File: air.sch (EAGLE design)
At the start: 30 parts, among them IC2 LM2937, Q1 FC-12M, Q2 FC-26M, Q3 BC849SMD, Q4 BC849SMD, U1 ESP8266, U2 W25Q32FV

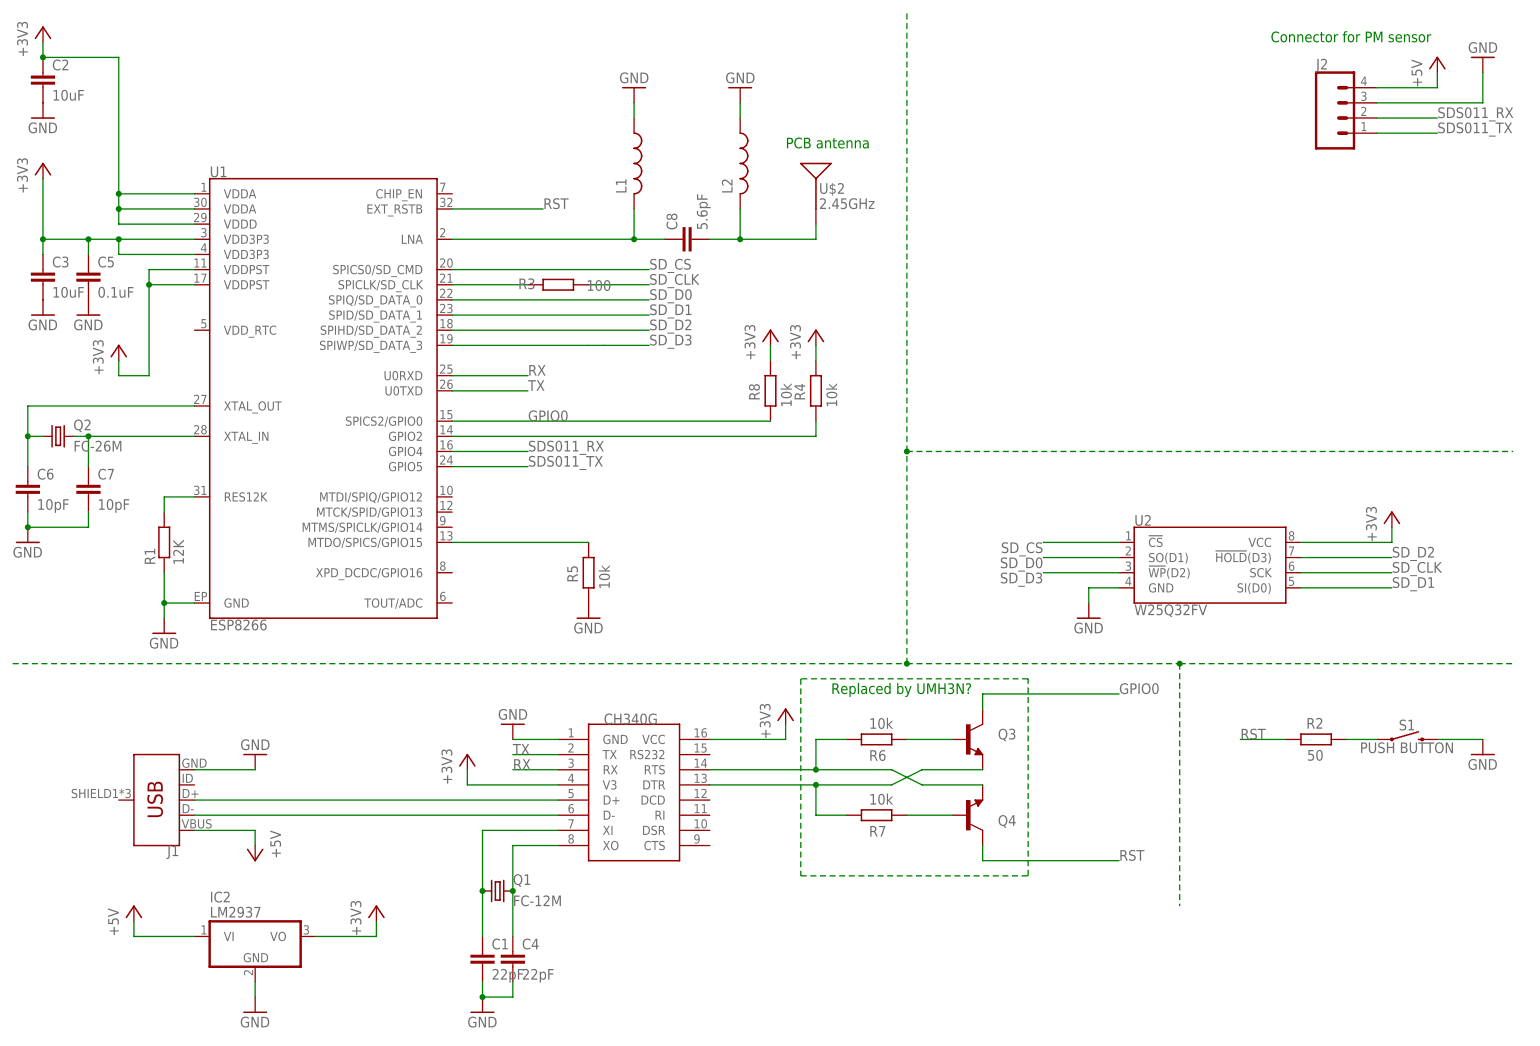
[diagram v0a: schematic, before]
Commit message: Switch to SMD, change voltage regulator, fix errors
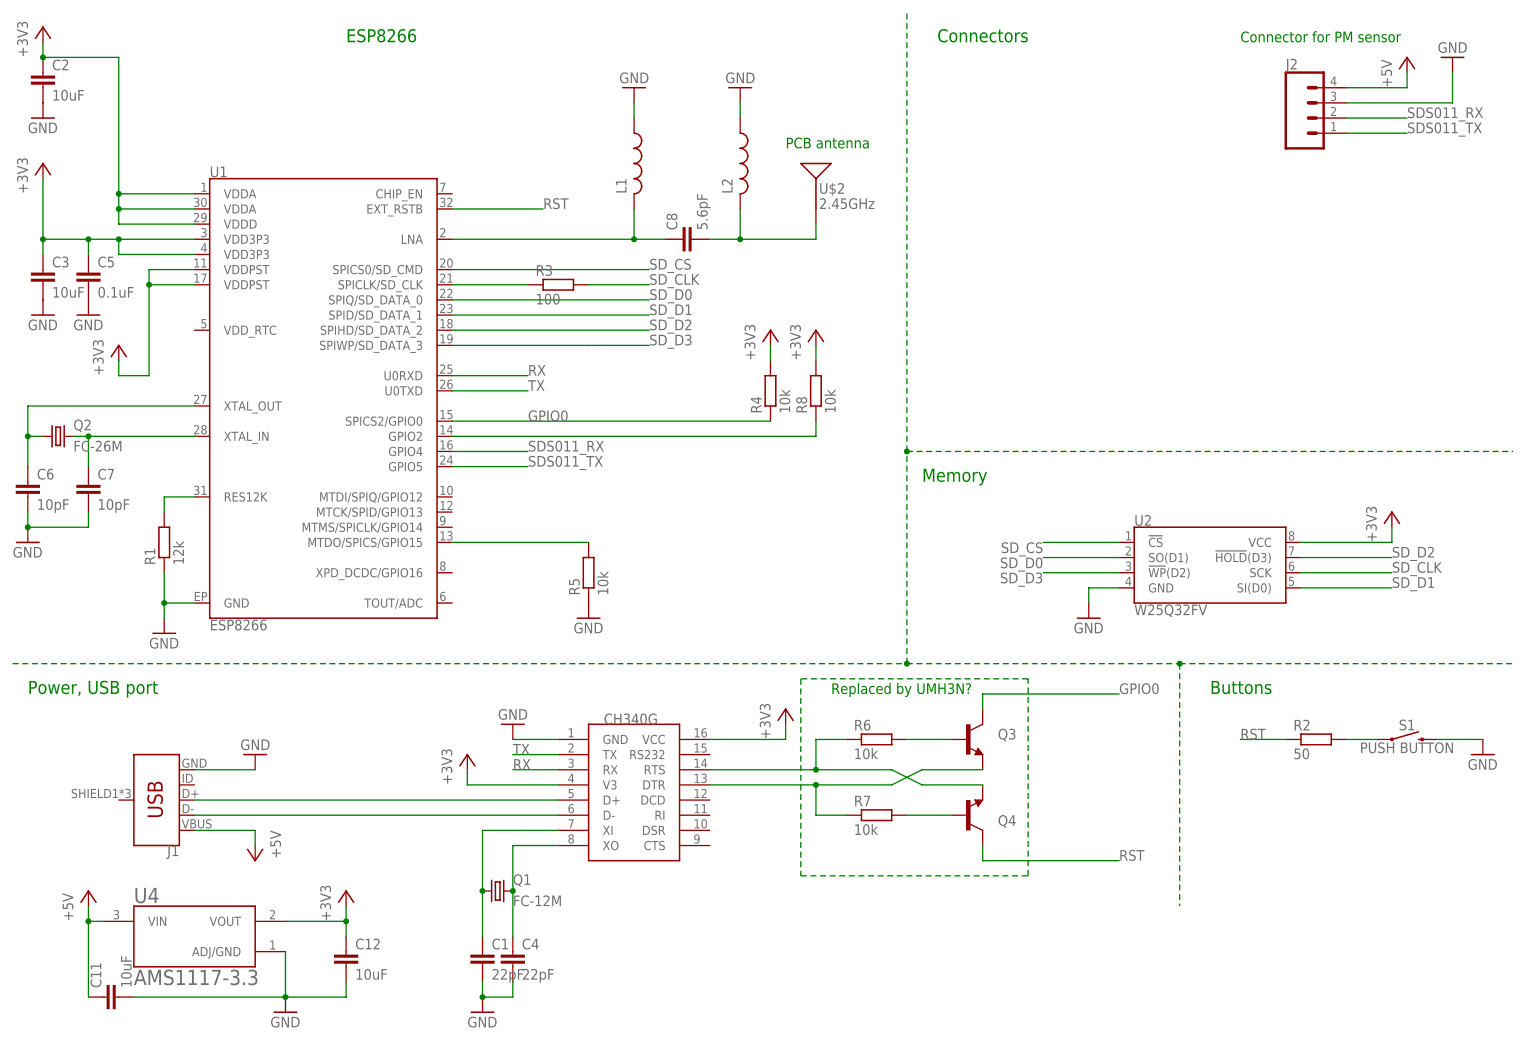
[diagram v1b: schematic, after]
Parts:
- removed IC2: LM2937, linear:LM2937
- added C11, C12: 10uF, rcl:C-EUC1206
- added U4: AMS1117-3.3, AMS1117-3.3:AMS1117-3.3
- L1, L2: device resistor:L-US0204/7 -> rcl:L-USL1812
- R1: value 12K -> 12k; device rcl:R-EU_0204/7 -> rcl:R-EU_R0805
- R2, R3, R4, R5, R6, R7, R8: device rcl:R-EU_0204/7 -> rcl:R-EU_R0805
- renumbered U$1 to U3
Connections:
- net +3V3: now also C12.1, R4.2, R8.2, U4.VOUT; no longer IC2.VO, R4.1, R8.1
- net +5V: now also C11.1, U4.VIN; no longer IC2.VI
- net GND: now also C11.2, C12.2, R5.1, U4.ADJ/GND; no longer IC2.GND, R5.2
- net GPIO0: now also R4.1; no longer R8.2
- net N$1: now also R3.1; no longer R3.2
- net N$12: now also R8.1; no longer R4.2
- net N$13: now also R5.2; no longer R5.1
- net N$9: now also R2.2; no longer R2.1
- net RST: now also R2.1; no longer R2.2
- net SD_CLK: now also R3.2; no longer R3.1
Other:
- note added: "Buttons"
- note added: "Connectors"
- note added: "ESP8266"
- note added: "Memory"
- note added: "Power, USB port"
- moved on the sheet: J2, R2, R3, R4, R5, R8

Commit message: Add capeboard schematic and led on main schematic
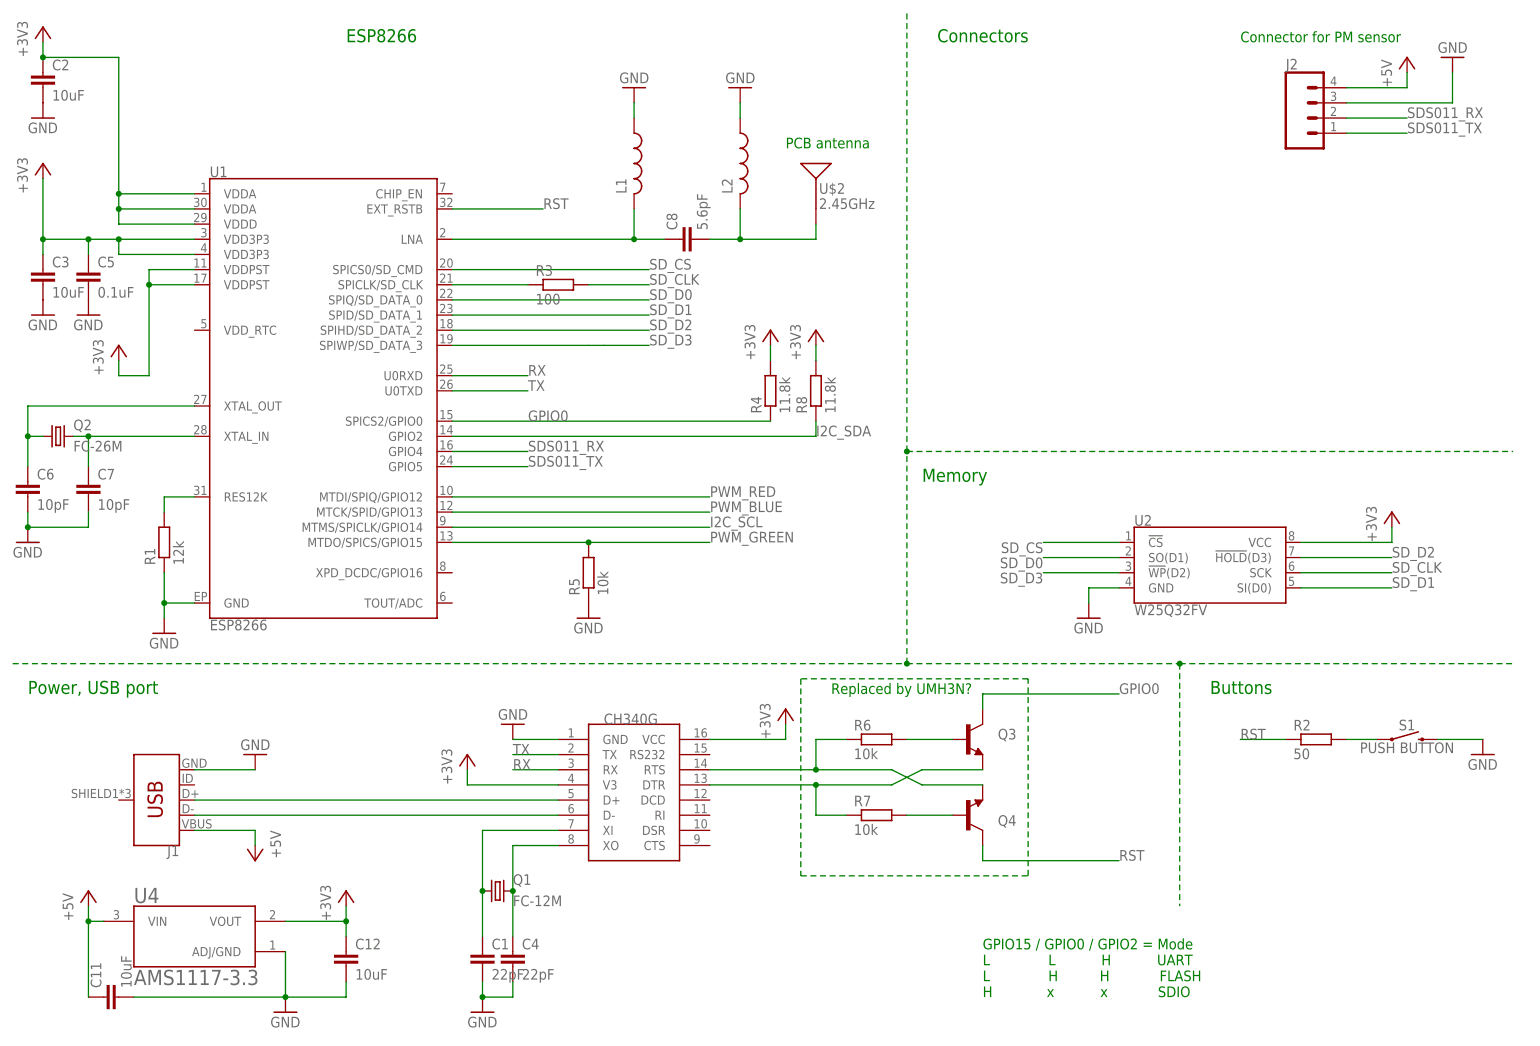
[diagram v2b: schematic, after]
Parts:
- R4, R8: value 10k -> 11.8k
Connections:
- net N$12 renamed I2C_SDA
- net N$13 renamed PWM_GREEN
- new net I2C_SCL: U1.MTMS/SPICLK/GPIO14
- new net PWM_RED: U1.MTDI/SPIQ/GPIO12
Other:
- note added: "GPIO15 / GPIO0 / GPIO2 = Mode L L H UART L H H FLASH H x x SDIO"
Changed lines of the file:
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@@
 <part name="GND15" library="supply1" library_urn="urn:adsk.eagle:library:371" deviceset="GND" device=""/>
 <part name="R3" library="rcl" library_urn="urn:adsk.eagle:library:334" deviceset="R-EU_" device="R0805" package3d_urn="urn:adsk.eagle:package:23553/2" value="100"/>
-<part name="R4" library="rcl" library_urn="urn:adsk.eagle:library:334" deviceset="R-EU_" device="R0805" package3d_urn="urn:adsk.eagle:package:23553/2" value="10k"/>
-<part name="R8" library="rcl" library_urn="urn:adsk.eagle:library:334" deviceset="R-EU_" device="R0805" package3d_urn="urn:adsk.eagle:package:23553/2" value="10k"/>
+<part name="R4" library="rcl" library_urn="urn:adsk.eagle:library:334" deviceset="R-EU_" device="R0805" package3d_urn="urn:adsk.eagle:package:23553/2" value="11.8k"/>
+<part name="R8" library="rcl" library_urn="urn:adsk.eagle:library:334" deviceset="R-EU_" device="R0805" package3d_urn="urn:adsk.eagle:package:23553/2" value="11.8k"/>
 <part name="R5" library="rcl" library_urn="urn:adsk.eagle:library:334" deviceset="R-EU_" device="R0805" package3d_urn="urn:adsk.eagle:package:23553/2" value="10k"/>
 <part name="R1" library="rcl" library_urn="urn:adsk.eagle:library:334" deviceset="R-EU_" device="R0805" package3d_urn="urn:adsk.eagle:package:23553/2" value="12k"/>
@@
 <text x="160.02" y="170.18" size="2.1844" layer="91">Connectors</text>
 <text x="205.74" y="60.96" size="2.1844" layer="91">Buttons</text>
+<text x="167.64" y="10.16" size="1.778" layer="91">GPIO15 / GPIO0 / GPIO2 = Mode
+L              L           H           UART
+L              H          H            FLASH
+H             x           x            SDIO</text>
 </plain>
 <instances>
@@
 </segment>
 </net>
-<net name="N$12" class="0">
+<net name="I2C_SDA" class="0">
 <segment>
 <pinref part="U1" gate="G$1" pin="GPIO2"/>
@@
 <wire x1="139.7" y1="104.14" x2="139.7" y2="106.68" width="0.1524" layer="91"/>
 <pinref part="R8" gate="G$1" pin="1"/>
-</segment>
-</net>
-<net name="N$13" class="0">
+<label x="139.7" y="104.14" size="1.778" layer="95"/>
+</segment>
+</net>
+<net name="PWM_GREEN" class="0">
 <segment>
 <pinref part="U1" gate="G$1" pin="MTDO/SPICS/GPIO15"/>
 <wire x1="78.74" y1="86.36" x2="101.6" y2="86.36" width="0.1524" layer="91"/>
 <pinref part="R5" gate="G$1" pin="2"/>
+<wire x1="101.6" y1="86.36" x2="121.92" y2="86.36" width="0.1524" layer="91"/>
+<junction x="101.6" y="86.36"/>
+<label x="121.92" y="86.36" size="1.778" layer="95"/>
 </segment>
 </net>
@@
 </segment>
 </net>
+<net name="PWM_RED" class="0">
+<segment>
+<pinref part="U1" gate="G$1" pin="MTDI/SPIQ/GPIO12"/>
+<wire x1="78.74" y1="93.98" x2="121.92" y2="93.98" width="0.1524" layer="91"/>
+<label x="121.92" y="93.98" size="1.778" layer="95"/>
+</segment>
+</net>
+<net name="PWM_BLUE" class="0">
+<segment>
+<wire x1="78.74" y1="91.44" x2="121.92" y2="91.44" width="0.1524" layer="91"/>
+<label x="121.92" y="91.44" size="1.778" layer="95"/>
+</segment>
+</net>
+<net name="I2C_SCL" class="0">
+<segment>
+<pinref part="U1" gate="G$1" pin="MTMS/SPICLK/GPIO14"/>
+<wire x1="78.74" y1="88.9" x2="121.92" y2="88.9" width="0.1524" layer="91"/>
+<label x="121.92" y="88.9" size="1.778" layer="95"/>
+</segment>
+</net>
 </nets>
 </sheet>
@@
 </drawing>
 <compatibility>
+<note version="6.3" minversion="6.2.2" severity="warning">
+Since Version 6.2.2 text objects can contain more than one line,
+which will not be processed correctly with this version.
+</note>
 <note version="8.2" severity="warning">
 Since Version 8.2, EAGLE supports online libraries. The ids
